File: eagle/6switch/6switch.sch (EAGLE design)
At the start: 13 parts, among them IC1 MCP23017SP, J1 RELAYBRD, Q1 BC548

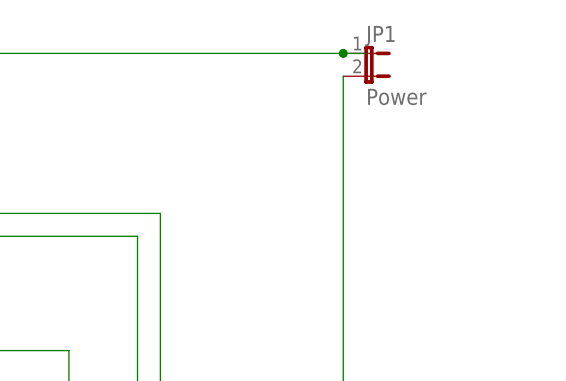
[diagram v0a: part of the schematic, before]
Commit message: changed some pin names
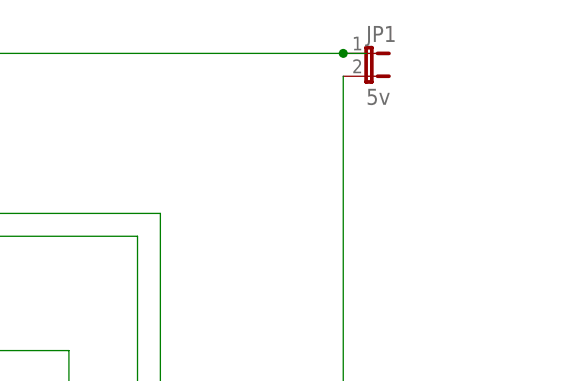
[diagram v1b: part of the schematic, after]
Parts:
- JP1: value Power -> 5v
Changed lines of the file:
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@@
 <part name="R2" library="eagle-ltspice" library_urn="urn:adsk.eagle:library:217" deviceset="R" device="0207/10" package3d_urn="urn:adsk.eagle:package:13275/1" value="4K7"/>
 <part name="J1" library="pinhead" library_urn="urn:adsk.eagle:library:325" deviceset="PINHD-1X8" device="" package3d_urn="urn:adsk.eagle:package:22409/2" value="RELAYBRD"/>
-<part name="JP1" library="jumper" library_urn="urn:adsk.eagle:library:252" deviceset="JP1E" device="" package3d_urn="urn:adsk.eagle:package:15455/1" value="Power"/>
+<part name="JP1" library="jumper" library_urn="urn:adsk.eagle:library:252" deviceset="JP1E" device="" package3d_urn="urn:adsk.eagle:package:15455/1" value="5v"/>
 <part name="X1" library="con-wago-500" library_urn="urn:adsk.eagle:library:195" deviceset="W237-102" device="" package3d_urn="urn:adsk.eagle:package:10688/1"/>
 <part name="X2" library="con-wago-500" library_urn="urn:adsk.eagle:library:195" deviceset="W237-102" device="" package3d_urn="urn:adsk.eagle:package:10688/1"/>

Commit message: eagle board
silkscreen stuff
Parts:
- X1: value (none) -> Sw1
- X2: value (none) -> Sw7
- X3: value (none) -> Sw5
- X4: value (none) -> Sw4
- X5: value (none) -> Sw3
- X6: value (none) -> Sw2
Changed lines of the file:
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@@
 <part name="J1" library="pinhead" library_urn="urn:adsk.eagle:library:325" deviceset="PINHD-1X8" device="" package3d_urn="urn:adsk.eagle:package:22409/2" value="RELAYBRD"/>
 <part name="JP1" library="jumper" library_urn="urn:adsk.eagle:library:252" deviceset="JP1E" device="" package3d_urn="urn:adsk.eagle:package:15455/1" value="5v"/>
-<part name="X1" library="con-wago-500" library_urn="urn:adsk.eagle:library:195" deviceset="W237-102" device="" package3d_urn="urn:adsk.eagle:package:10688/1"/>
-<part name="X2" library="con-wago-500" library_urn="urn:adsk.eagle:library:195" deviceset="W237-102" device="" package3d_urn="urn:adsk.eagle:package:10688/1"/>
-<part name="X3" library="con-wago-500" library_urn="urn:adsk.eagle:library:195" deviceset="W237-102" device="" package3d_urn="urn:adsk.eagle:package:10688/1"/>
-<part name="X4" library="con-wago-500" library_urn="urn:adsk.eagle:library:195" deviceset="W237-102" device="" package3d_urn="urn:adsk.eagle:package:10688/1"/>
-<part name="X5" library="con-wago-500" library_urn="urn:adsk.eagle:library:195" deviceset="W237-102" device="" package3d_urn="urn:adsk.eagle:package:10688/1"/>
-<part name="X6" library="con-wago-500" library_urn="urn:adsk.eagle:library:195" deviceset="W237-102" device="" package3d_urn="urn:adsk.eagle:package:10688/1"/>
+<part name="X1" library="con-wago-500" library_urn="urn:adsk.eagle:library:195" deviceset="W237-102" device="" package3d_urn="urn:adsk.eagle:package:10688/1" value="Sw1"/>
+<part name="X2" library="con-wago-500" library_urn="urn:adsk.eagle:library:195" deviceset="W237-102" device="" package3d_urn="urn:adsk.eagle:package:10688/1" value="Sw7"/>
+<part name="X3" library="con-wago-500" library_urn="urn:adsk.eagle:library:195" deviceset="W237-102" device="" package3d_urn="urn:adsk.eagle:package:10688/1" value="Sw5"/>
+<part name="X4" library="con-wago-500" library_urn="urn:adsk.eagle:library:195" deviceset="W237-102" device="" package3d_urn="urn:adsk.eagle:package:10688/1" value="Sw4"/>
+<part name="X5" library="con-wago-500" library_urn="urn:adsk.eagle:library:195" deviceset="W237-102" device="" package3d_urn="urn:adsk.eagle:package:10688/1" value="Sw3"/>
+<part name="X6" library="con-wago-500" library_urn="urn:adsk.eagle:library:195" deviceset="W237-102" device="" package3d_urn="urn:adsk.eagle:package:10688/1" value="Sw2"/>
 </parts>
 <sheets>
@@
 </sheet>
 </sheets>
+<errors>
+</errors>
 </schematic>
 </drawing>

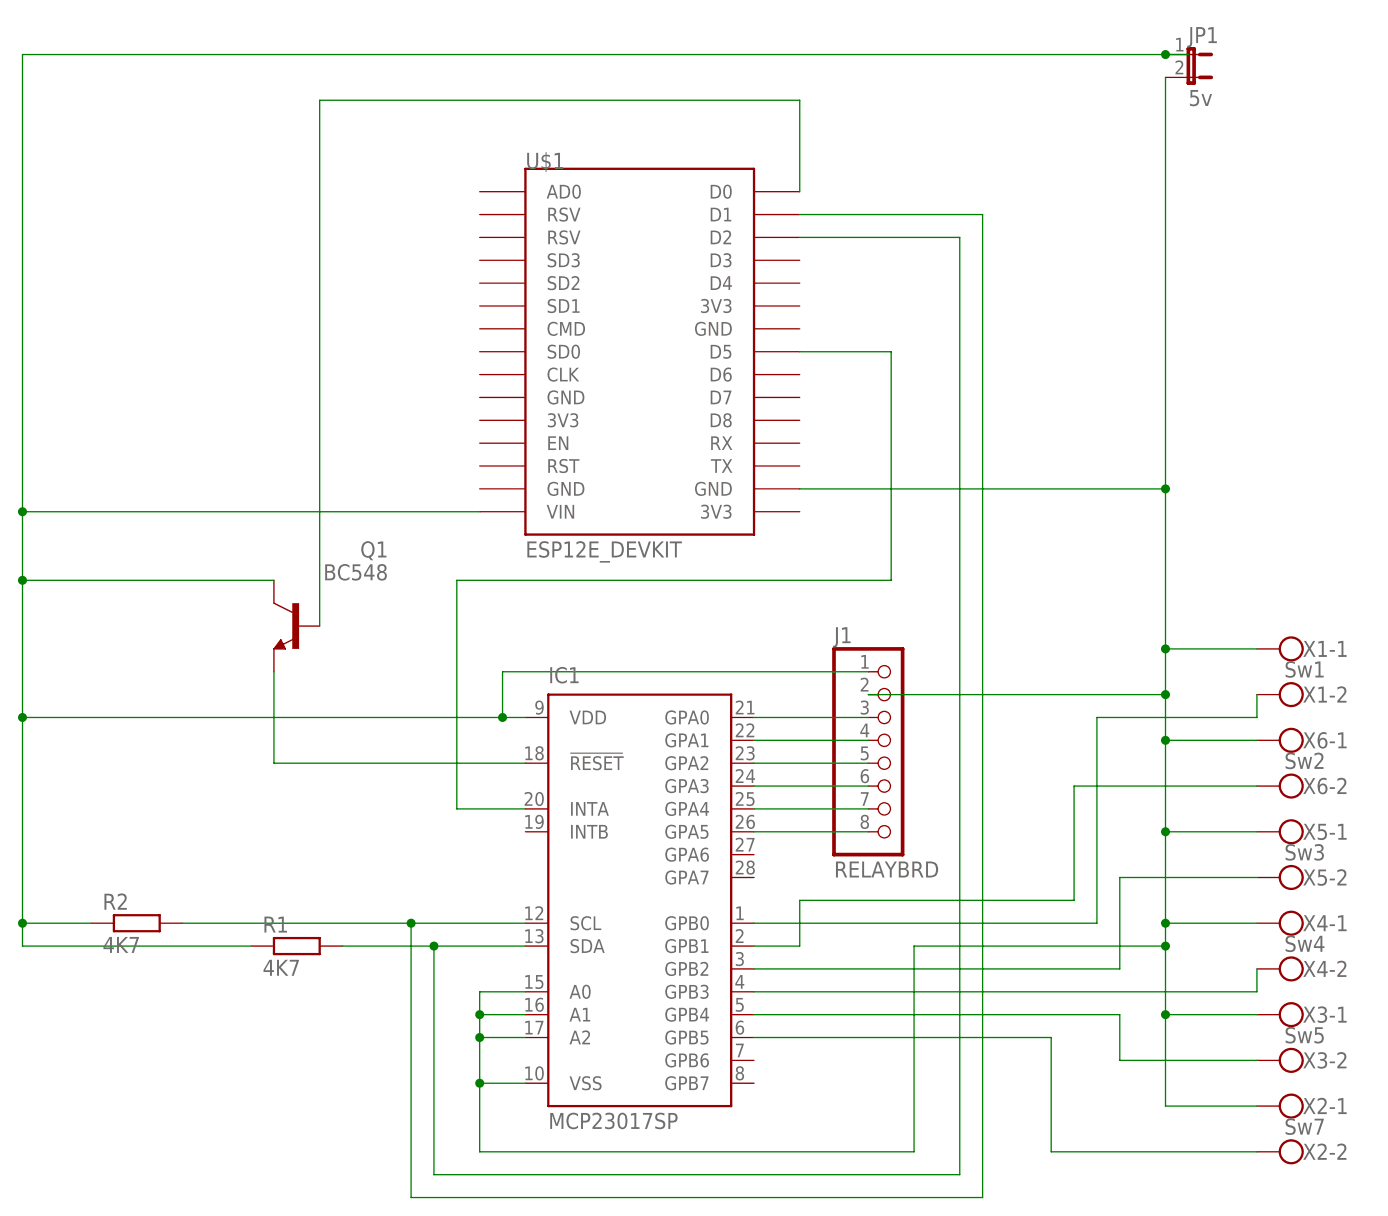
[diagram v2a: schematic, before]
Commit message: added a 'power down the relay board' tranisistor, more debug, changed types to be more uniform, added a tarpit delay to the web commands, and a minimum time between relays, multiple commands can now be sent on the web api, fixed the NODEMCU size in the board, and the miswired A/B IOs on the MCP
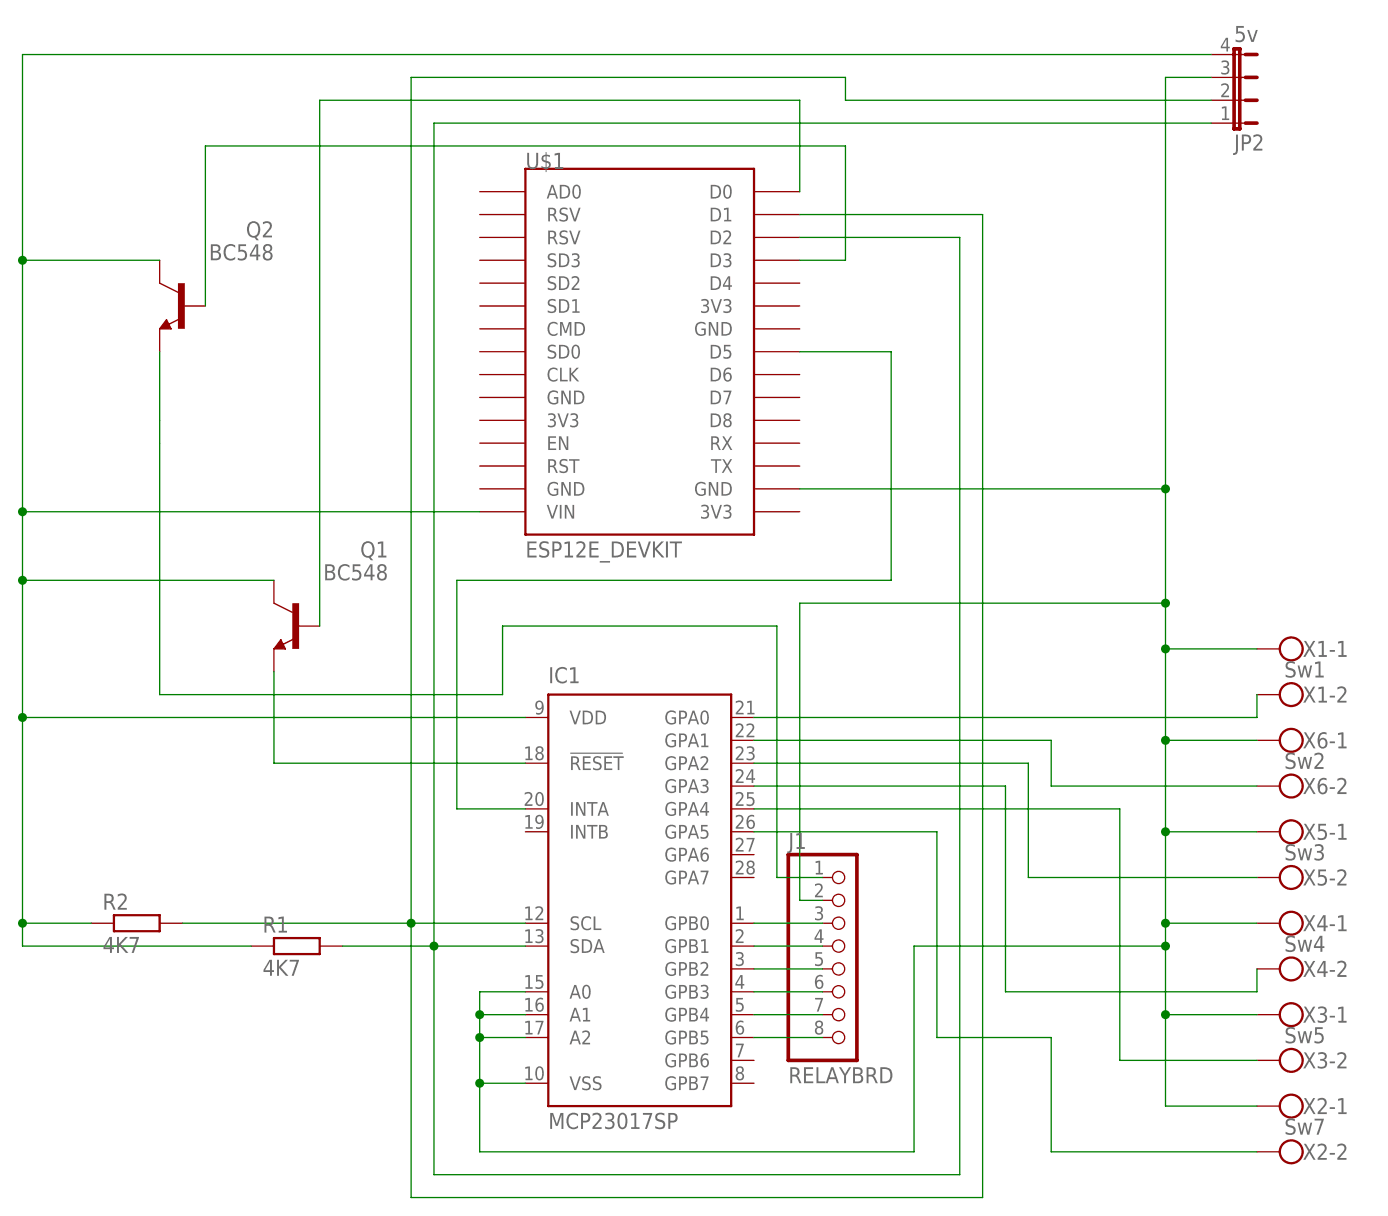
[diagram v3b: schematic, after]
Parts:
- removed JP1: 5v, jumper:JP1E
- added JP2: 5v, jumper:JP4E
- added Q2: BC548, transistor-npn:BC548
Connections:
- new net SCL: IC1.SCL, JP2.2, R2.2, U$1.D1
- new net SDA: IC1.SDA, JP2.1, R1.2, U$1.D2
- net GND: now also JP2.3; no longer JP1.2
- net N$10: now also X1-2.KL; no longer J1.3
- net N$11: now also IC1.GPB1; no longer IC1.GPA1
- net N$12: now also IC1.GPB2; no longer IC1.GPA2
- net N$13: now also IC1.GPB3; no longer IC1.GPA3
- net N$14: now also IC1.GPB4; no longer IC1.GPA4
- net N$15: now also IC1.GPB5; no longer IC1.GPA5
- net N$16: now also IC1.GPA4; no longer IC1.GPB4
- net N$17: now also IC1.GPA5; no longer IC1.GPB5
- net N$3: now also J1.1, Q2.E; no longer IC1.SCL, R2.2, U$1.D1
- net N$4: now also Q2.B, U$1.D3; no longer IC1.SDA, R1.2, U$1.D2
- net N$5: now also IC1.GPA1, X6-2.KL; no longer IC1.GPB0, X1-2.KL
- net N$6: now also IC1.GPB0, J1.3; no longer IC1.GPB1, X6-2.KL
- net N$8: now also IC1.GPA2; no longer IC1.GPB2
- net N$9: now also IC1.GPA3; no longer IC1.GPB3
- net VCC: now also JP2.4, Q2.C; no longer J1.1, JP1.1
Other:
- moved on the sheet: J1
